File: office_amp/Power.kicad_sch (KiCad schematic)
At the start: 19 parts, among them J1 Jack-DC, Q1 DMT6012LSS, U1 LM74700, U2 TBA_2-2421, U4 TBA_2-2421

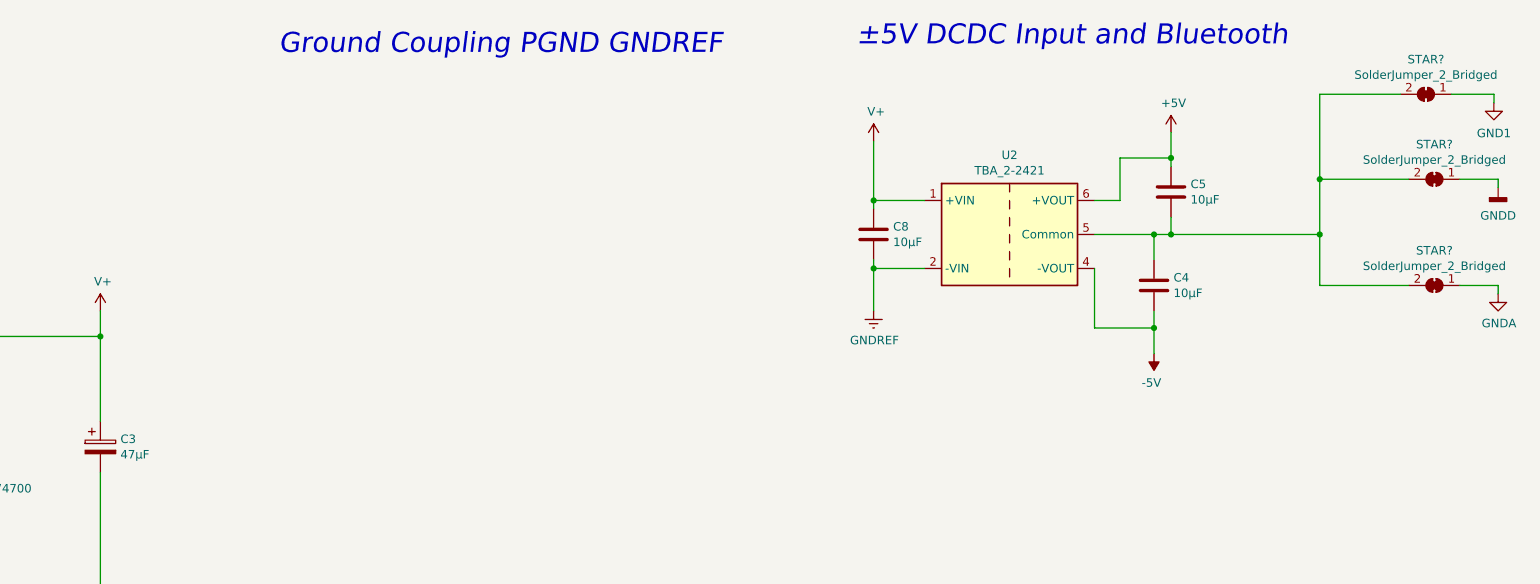
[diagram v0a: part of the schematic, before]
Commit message: Changed Components to available parts
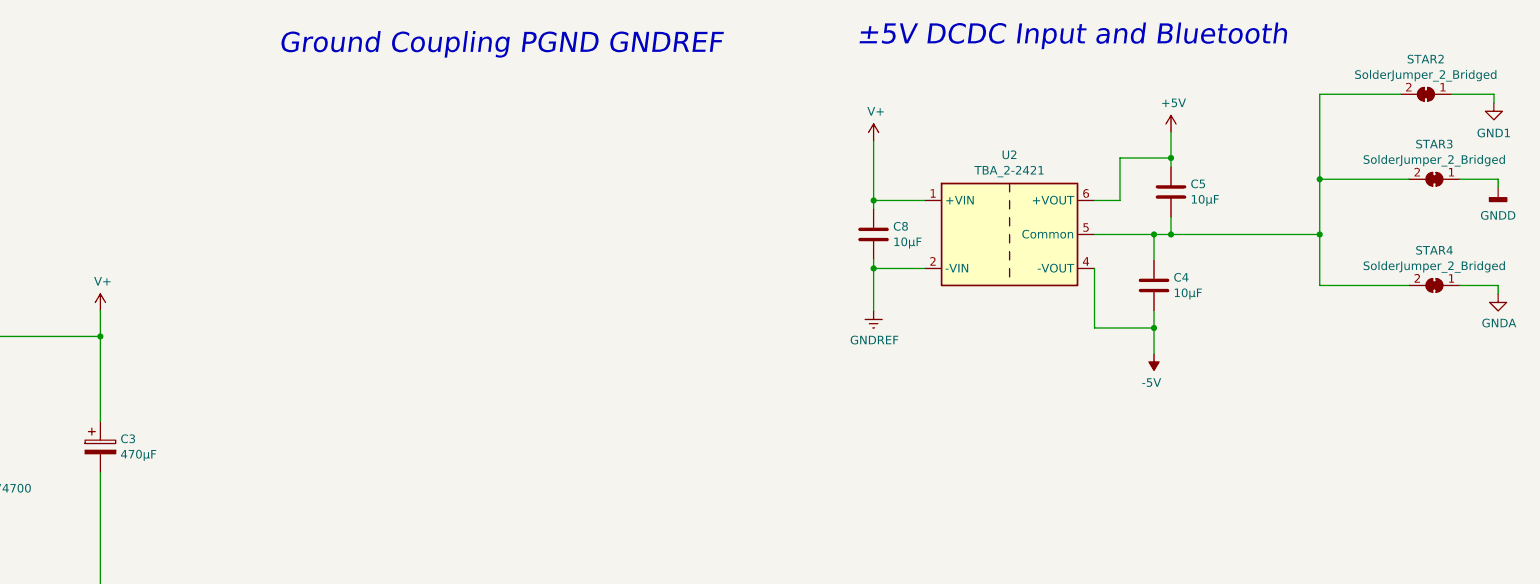
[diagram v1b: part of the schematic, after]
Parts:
- C3: value 47µF -> 470µF; footprint Capacitor_THT:CP_Radial_D5.0mm_P2.00mm -> Capacitor_THT:CP_Radial_D10.0mm_P5.00mm
- gave numbers to parts that had none: 3
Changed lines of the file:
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@@
       (effects (font (size 1.27 1.27)) (justify left))
     )
-    (property "Value" "47µF" (id 1) (at 116.0272 87.503 0)
-      (effects (font (size 1.27 1.27)) (justify left))
-    )
-    (property "Footprint" "Capacitor_THT:CP_Radial_D5.0mm_P2.00mm" (id 2) (at 113.9952 90.17 0)
+    (property "Value" "470µF" (id 1) (at 116.0272 87.503 0)
+      (effects (font (size 1.27 1.27)) (justify left))
+    )
+    (property "Footprint" "Capacitor_THT:CP_Radial_D10.0mm_P5.00mm" (id 2) (at 113.9952 90.17 0)
       (effects (font (size 1.27 1.27)) hide)
     )
@@
   (symbol (lib_id "power:GNDD") (at 321.945 47.625 0) (unit 1)
     (in_bom yes) (on_board yes) (fields_autoplaced)
-    (property "Reference" "#PWR?" (id 0) (at 321.945 53.975 0)
+    (property "Reference" "#PWR022" (id 0) (at 321.945 53.975 0)
       (effects (font (size 1.27 1.27)) hide)
     )
@@
   (symbol (lib_id "power:GND1") (at 321.31 34.925 0) (unit 1)
     (in_bom yes) (on_board yes) (fields_autoplaced)
-    (property "Reference" "#PWR?" (id 0) (at 321.31 41.275 0)
+    (property "Reference" "#PWR01" (id 0) (at 321.31 41.275 0)
       (effects (font (size 1.27 1.27)) hide)
     )
@@
   (symbol (lib_id "Jumper:SolderJumper_2_Bridged") (at 312.42 62.23 0) (mirror y) (unit 1)
     (in_bom yes) (on_board yes)
-    (property "Reference" "STAR?" (id 0) (at 312.42 57.023 0))
+    (property "Reference" "STAR4" (id 0) (at 312.42 57.023 0))
     (property "Value" "SolderJumper_2_Bridged" (id 1) (at 312.42 59.3344 0))
     (property "Footprint" "Jumper:SolderJumper-2_P1.3mm_Bridged_RoundedPad1.0x1.5mm" (id 2) (at 312.42 62.23 0)
@@
   (symbol (lib_id "Jumper:SolderJumper_2_Bridged") (at 312.42 46.355 0) (mirror y) (unit 1)
     (in_bom yes) (on_board yes)
-    (property "Reference" "STAR?" (id 0) (at 312.42 41.148 0))
+    (property "Reference" "STAR3" (id 0) (at 312.42 41.148 0))
     (property "Value" "SolderJumper_2_Bridged" (id 1) (at 312.42 43.4594 0))
     (property "Footprint" "Jumper:SolderJumper-2_P1.3mm_Bridged_RoundedPad1.0x1.5mm" (id 2) (at 312.42 46.355 0)
@@
   (symbol (lib_id "Jumper:SolderJumper_2_Bridged") (at 311.15 33.655 0) (mirror y) (unit 1)
     (in_bom yes) (on_board yes)
-    (property "Reference" "STAR?" (id 0) (at 311.15 28.448 0))
+    (property "Reference" "STAR2" (id 0) (at 311.15 28.448 0))
     (property "Value" "SolderJumper_2_Bridged" (id 1) (at 311.15 30.7594 0))
     (property "Footprint" "Jumper:SolderJumper-2_P1.3mm_Bridged_RoundedPad1.0x1.5mm" (id 2) (at 311.15 33.655 0)

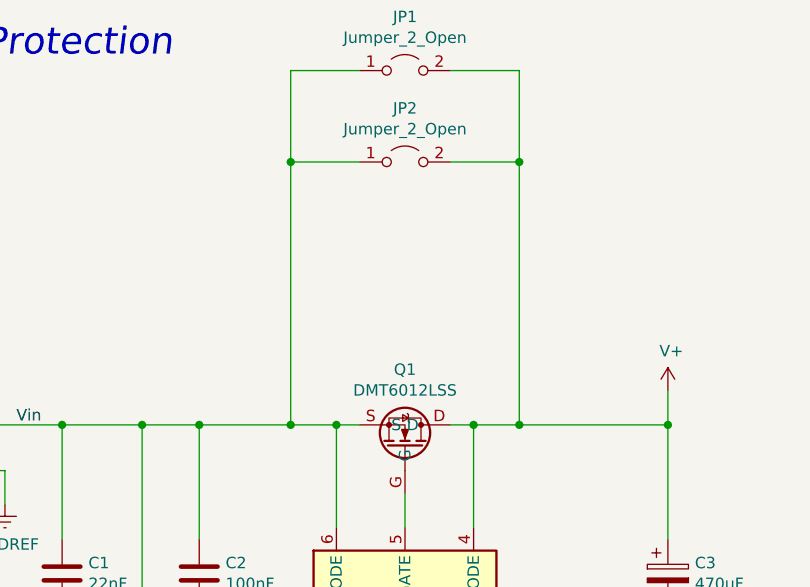
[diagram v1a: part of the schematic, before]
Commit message: First positioning of new components (top site), added mounting holes for case  compabillity (Donau 523178)
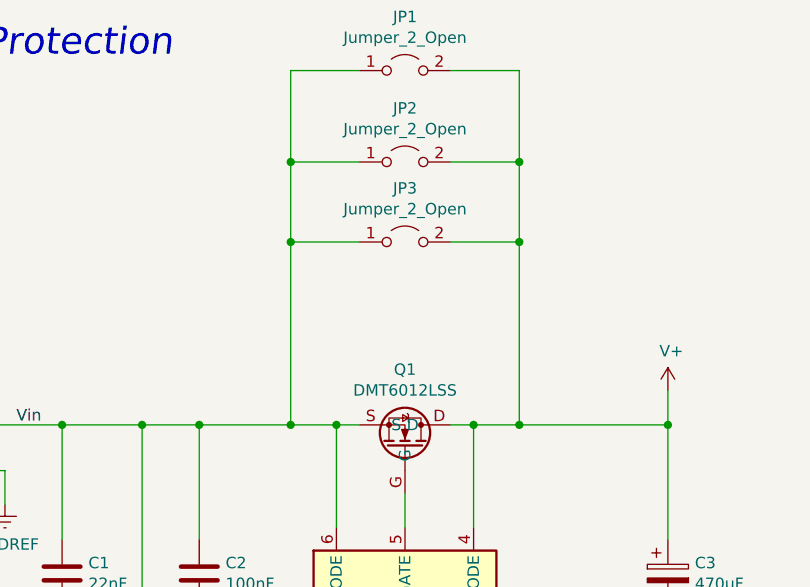
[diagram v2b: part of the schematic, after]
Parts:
- added JP3: Jumper_2_Open, Jumper:SolderJumper-2_P1.3mm_Open_TrianglePad1.0x1.5mm, symbol Jumper:Jumper_2_Open
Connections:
- net V+: now also JP3.2 (B)
- net Vin: now also JP3.1 (A)
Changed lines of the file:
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@@
   (junction (at 295.275 54.61) (diameter 0) (color 0 0 0 0)
   )
+  (junction (at 96.52 49.53) (diameter 0) (color 0 0 0 0)
+  )
   (junction (at 222.885 170.18) (diameter 0) (color 0 0 0 0)
   )
@@
   (junction (at 295.275 46.355) (diameter 0) (color 0 0 0 0)
   )
+  (junction (at 71.12 49.53) (diameter 0) (color 0 0 0 0)
+  )
   (junction (at 96.52 40.64) (diameter 0) (color 0 0 0 0)
   )
@@
     (stroke (width 0) (type default) (color 0 0 0 0))
   )
-  (wire (pts (xy 71.12 40.64) (xy 71.12 69.85))
+  (wire (pts (xy 71.12 40.64) (xy 71.12 49.53))
     (stroke (width 0) (type default) (color 0 0 0 0))
   )
@@
     (stroke (width 0) (type default) (color 0 0 0 0))
   )
+  (wire (pts (xy 71.12 49.53) (xy 78.74 49.53))
+    (stroke (width 0) (type default) (color 0 0 0 0))
+  )
   (wire (pts (xy 228.6 59.69) (xy 236.22 59.69))
     (stroke (width 0) (type default) (color 0 0 0 0))
@@
     (stroke (width 0) (type default) (color 0 0 0 0))
   )
+  (wire (pts (xy 71.12 49.53) (xy 71.12 69.85))
+    (stroke (width 0) (type default) (color 0 0 0 0))
+  )
   (wire (pts (xy 316.23 62.23) (xy 321.945 62.23))
     (stroke (width 0) (type default) (color 0 0 0 0))
@@
     (stroke (width 0) (type default) (color 0 0 0 0))
   )
+  (wire (pts (xy 96.52 49.53) (xy 96.52 69.85))
+    (stroke (width 0) (type default) (color 0 0 0 0))
+  )
   (wire (pts (xy 96.52 30.48) (xy 96.52 40.64))
     (stroke (width 0) (type default) (color 0 0 0 0))
   )
+  (wire (pts (xy 88.9 49.53) (xy 96.52 49.53))
+    (stroke (width 0) (type default) (color 0 0 0 0))
+  )
   (wire (pts (xy 228.6 49.53) (xy 228.6 50.8))
     (stroke (width 0) (type default) (color 0 0 0 0))
@@
     (stroke (width 0) (type default) (color 0 0 0 0))
   )
-  (wire (pts (xy 96.52 40.64) (xy 96.52 69.85))
+  (wire (pts (xy 96.52 40.64) (xy 96.52 49.53))
     (stroke (width 0) (type default) (color 0 0 0 0))
   )
@@
     (pin "1")
   )
+  (symbol (lib_id "Jumper:Jumper_2_Open") (at 83.82 49.53 0) (unit 1)
+    (in_bom yes) (on_board yes)
+    (property "Reference" "JP3" (id 0) (at 83.82 43.561 0))
+    (property "Value" "Jumper_2_Open" (id 1) (at 83.82 45.8724 0))
+    (property "Footprint" "Jumper:SolderJumper-2_P1.3mm_Open_TrianglePad1.0x1.5mm" (id 2) (at 83.82 49.53 0)
+      (effects (font (size 1.27 1.27)) hide)
+    )
+    (property "Datasheet" "~" (id 3) (at 83.82 49.53 0)
+      (effects (font (size 1.27 1.27)) hide)
+    )
+    (pin "1")
+    (pin "2")
+  )
   (symbol (lib_id "power:GND1") (at 321.31 34.925 0) (unit 1)

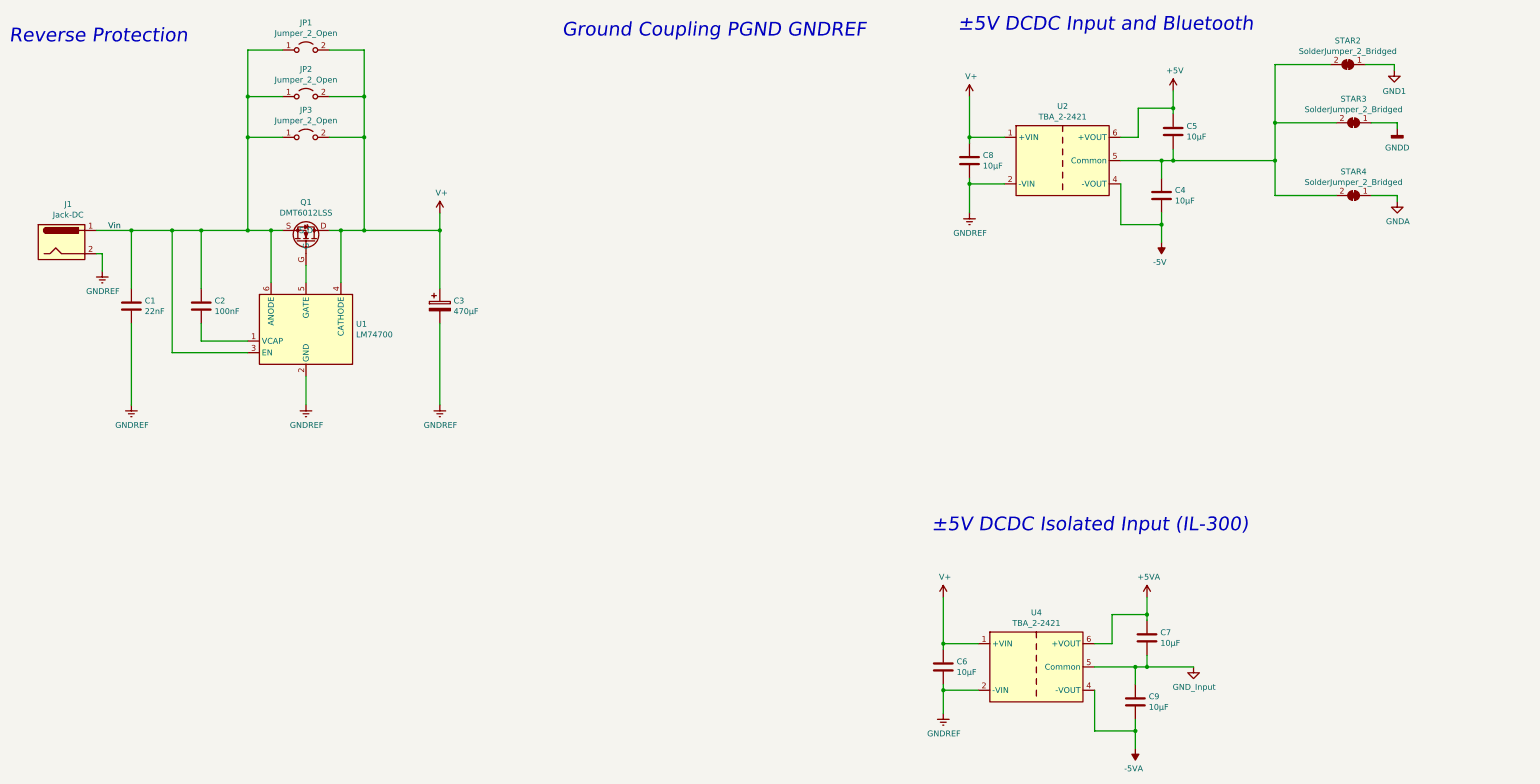
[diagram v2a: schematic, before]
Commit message: added testpoints, corrected footprints, removed ground loop dgnd gnda
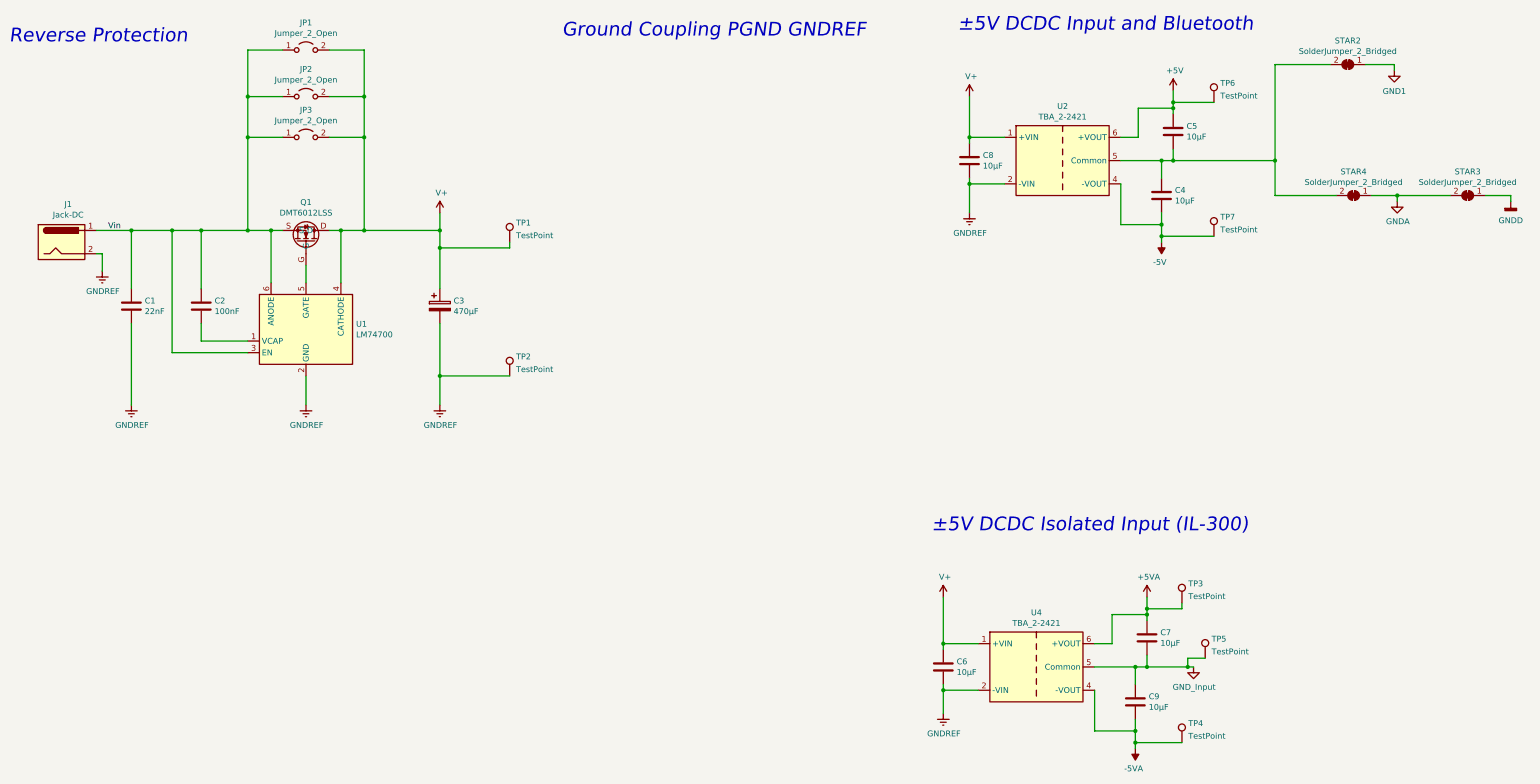
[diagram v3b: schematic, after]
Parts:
- added TP1, TP3, TP4, TP6, TP7: TestPoint, TestPoint:TestPoint_Pad_D1.0mm, symbol Connector:TestPoint
- added TP2, TP5: TestPoint, TestPoint:TestPoint_Loop_D2.60mm_Drill1.4mm_Beaded, symbol Connector:TestPoint
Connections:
- net +5V: now also TP6.1
- net +5VA: now also TP3.1
- net -5V: now also TP7.1
- net -5VA: now also TP4.1
- net GNDA: now also STAR3.2 (B)
- net GNDREF: now also TP2.1
- net GND_Input: now also TP5.1
- net V+: now also TP1.1
- net at C4.1, C5.2, STAR2.2 (B)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: no longer STAR3.2 (B)
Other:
- moved on the sheet: STAR3

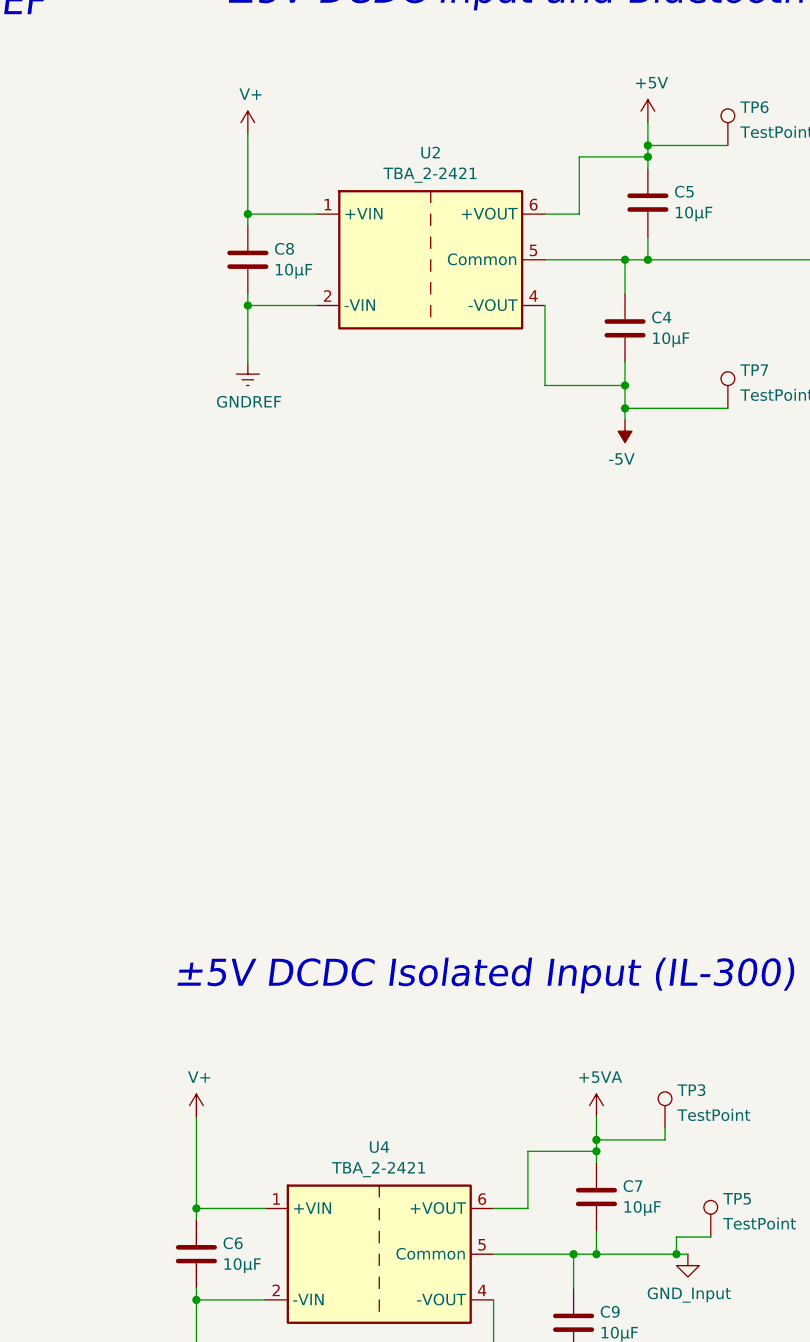
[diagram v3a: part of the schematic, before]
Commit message: First layout touch interface
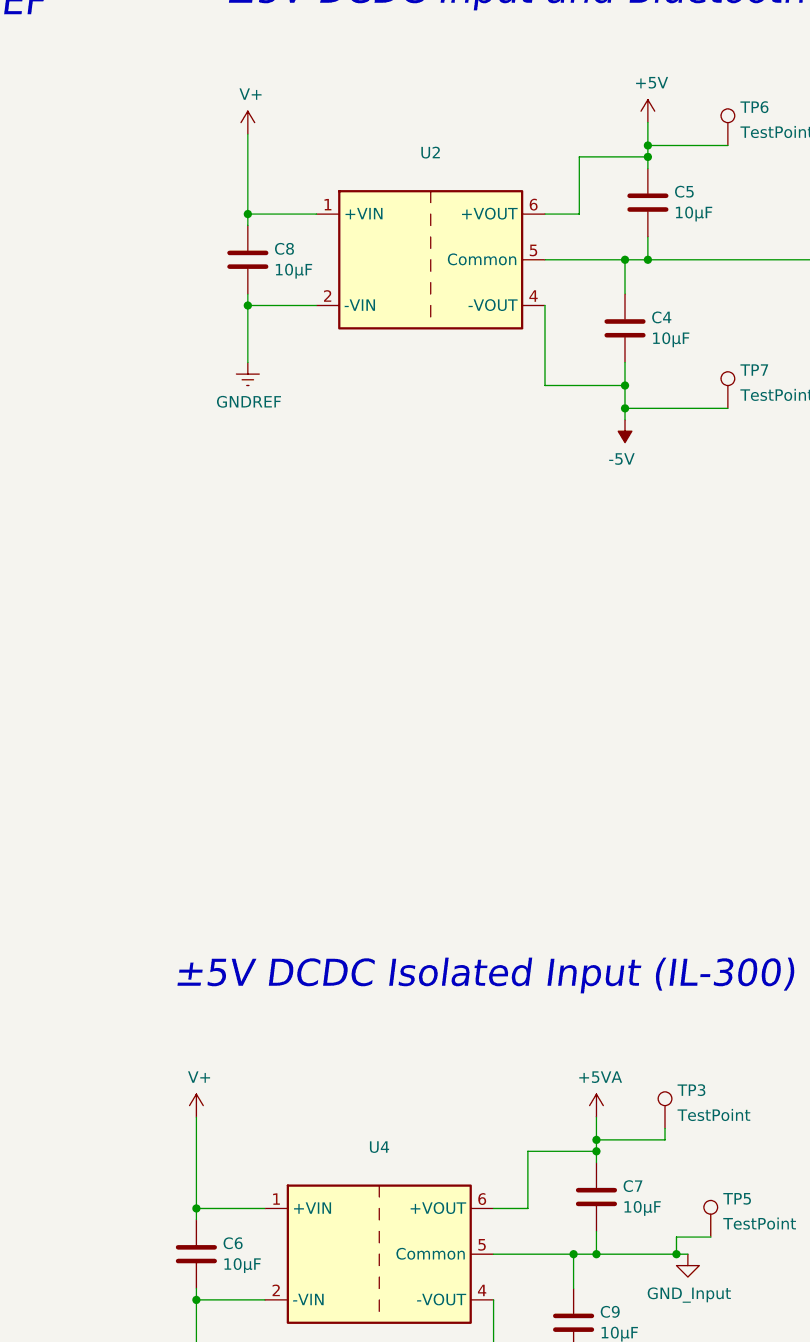
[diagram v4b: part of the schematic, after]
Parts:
- U2, U4: value TBA_2-2421 -> (none); footprint MyLib:SIP-7 -> (none)
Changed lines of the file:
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@@
     (in_bom yes) (on_board yes)
     (property "Reference" "U4" (id 0) (at 243.205 153.2382 0))
-    (property "Value" "TBA_2-2421" (id 1) (at 243.205 155.5496 0))
-    (property "Footprint" "MyLib:SIP-7" (id 2) (at 243.205 173.99 0)
+    (property "Value" "" (id 1) (at 243.205 155.5496 0))
+    (property "Footprint" "" (id 2) (at 243.205 173.99 0)
       (effects (font (size 1.27 1.27)) hide)
     )
@@
     (in_bom yes) (on_board yes)
     (property "Reference" "U2" (id 0) (at 248.92 42.7482 0))
-    (property "Value" "TBA_2-2421" (id 1) (at 248.92 45.0596 0))
-    (property "Footprint" "MyLib:SIP-7" (id 2) (at 248.92 63.5 0)
+    (property "Value" "" (id 1) (at 248.92 45.0596 0))
+    (property "Footprint" "" (id 2) (at 248.92 63.5 0)
       (effects (font (size 1.27 1.27)) hide)
     )

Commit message: Changes from testing
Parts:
- U2, U4: value (none) -> TBA_2-2421; footprint (none) -> office_amp:SIP-7
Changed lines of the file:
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@@
     (in_bom yes) (on_board yes)
     (property "Reference" "U4" (id 0) (at 243.205 153.2382 0))
-    (property "Value" "" (id 1) (at 243.205 155.5496 0))
-    (property "Footprint" "" (id 2) (at 243.205 173.99 0)
+    (property "Value" "TBA_2-2421" (id 1) (at 243.205 155.5496 0))
+    (property "Footprint" "office_amp:SIP-7" (id 2) (at 243.205 173.99 0)
       (effects (font (size 1.27 1.27)) hide)
     )
@@
     (in_bom yes) (on_board yes)
     (property "Reference" "U2" (id 0) (at 248.92 42.7482 0))
-    (property "Value" "" (id 1) (at 248.92 45.0596 0))
-    (property "Footprint" "" (id 2) (at 248.92 63.5 0)
+    (property "Value" "TBA_2-2421" (id 1) (at 248.92 45.0596 0))
+    (property "Footprint" "office_amp:SIP-7" (id 2) (at 248.92 63.5 0)
       (effects (font (size 1.27 1.27)) hide)
     )
